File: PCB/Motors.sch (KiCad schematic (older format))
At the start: 8 parts, among them J1 Conn_01x06, J2 Conn_01x06, U1 ROB-14450

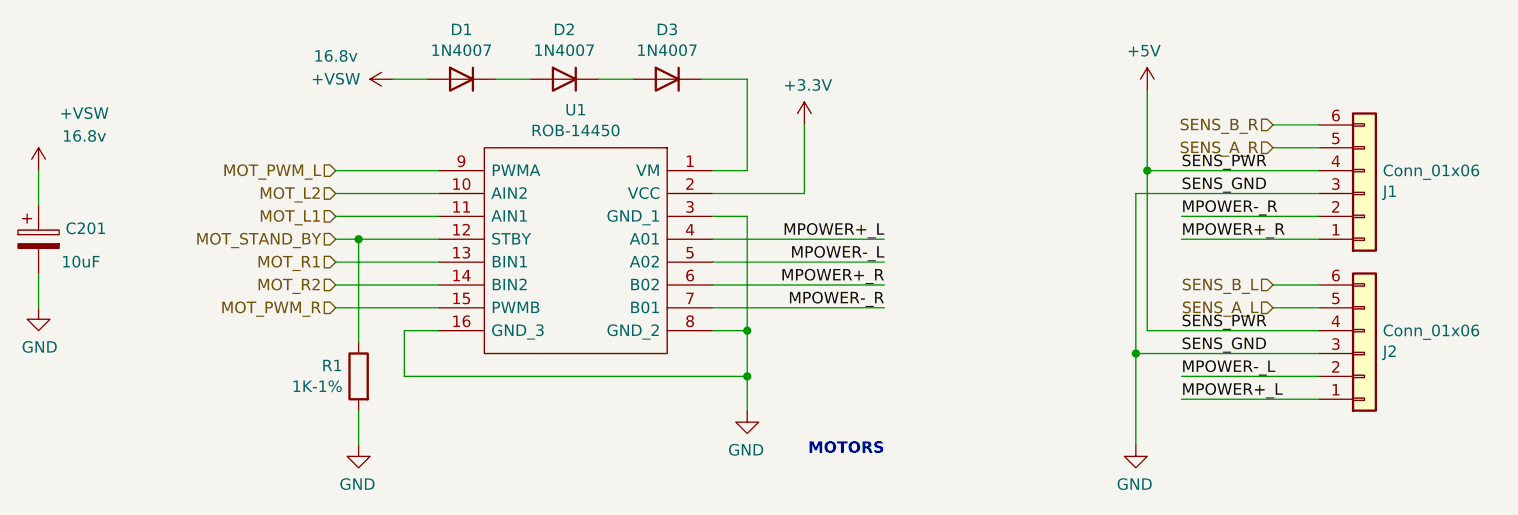
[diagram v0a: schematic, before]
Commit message: Refactor Firmware and implement serial communication
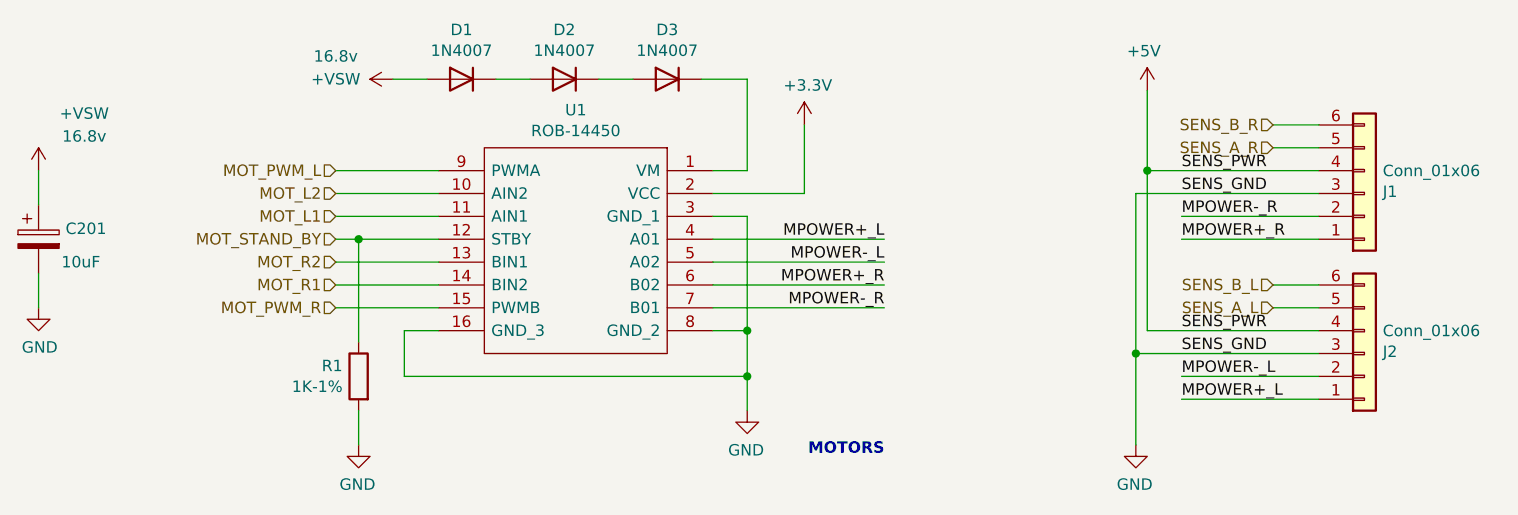
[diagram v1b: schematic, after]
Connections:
- net MOT_R1: now also U1.14 (BIN2); no longer U1.13 (BIN1)
- net MOT_R2: now also U1.13 (BIN1); no longer U1.14 (BIN2)
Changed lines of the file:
@@
 Text HLabel 3850 3650 0    50   Input ~ 0
 MOT_L1
+Text HLabel 3850 3950 0    50   Input ~ 0
+MOT_R1
 Text HLabel 3850 3850 0    50   Input ~ 0
-MOT_R1
-Text HLabel 3850 3950 0    50   Input ~ 0
 MOT_R2
 Wire Wire Line
